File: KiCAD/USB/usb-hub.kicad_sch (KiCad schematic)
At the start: 3 parts, among them J1 Conn_01x10_Pin, J2 Conn_01x10_Pin, J3 Conn_01x04_Socket

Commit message: mmmm... usb hub controller...
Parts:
- added C1, C2, C3, C4, C5: 0.1μF, symbol Device:C_Small
- added C6: 4.7μF, symbol Device:C_Small
- added R1: 649Ω, symbol Device:R_Small
- added R2, R3, R4, R5: 10kΩ, symbol Device:R_Small
- added U1: CY7C65634-28LTXC, QFN-28, symbol 2025-09-11_12-45-01:CY7C65634-28LTXC
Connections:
- net GND: now also R1.2, U1.22 (SELFPWR), U1.29
- net USB_FNG_N: now also U1.6 (DD-[2])
- net USB_FNG_P: now also U1.7 (DD+[2])
- net USB_HOST_N: now also U1.1 (D-)
- net USB_HOST_P: now also U1.2 (D+)
- net USB_KB_N: now also U1.3 (D0-[1])
- net USB_KB_P: now also U1.4 (D0+[1])
- net VBUS: now also C6.2
- new net: R3.1, U1.23 (GANG)
- new net: C3.2, U1.9 (VCC_A)
- new net: R1.1, U1.8 (RREF)
- new net: C2.1, U1.5 (VCC_A)
- new net: R5.2, U1.24 (*OVR[2])
- new net: R4.1, U1.25 (*OVR[1])
- new net: C5.2, C6.1
- new net: C5.1, U1.27 (VCC)
- new net: R2.1, U1.17 (*RESET)
- new net: C4.1, U1.14 (VCC_A)
- new net: C1.1, U1.21 (VCC_D)
- new net +3V3: C1.2, C2.2, C3.1, C4.2, R2.2, R3.2, R4.2, R5.1, U1.28 (VREG)
- new net X_IN: U1.10 (XIN)
- new net X_OUT: U1.11 (XOUT)
- no-connect marks 0 -> 2

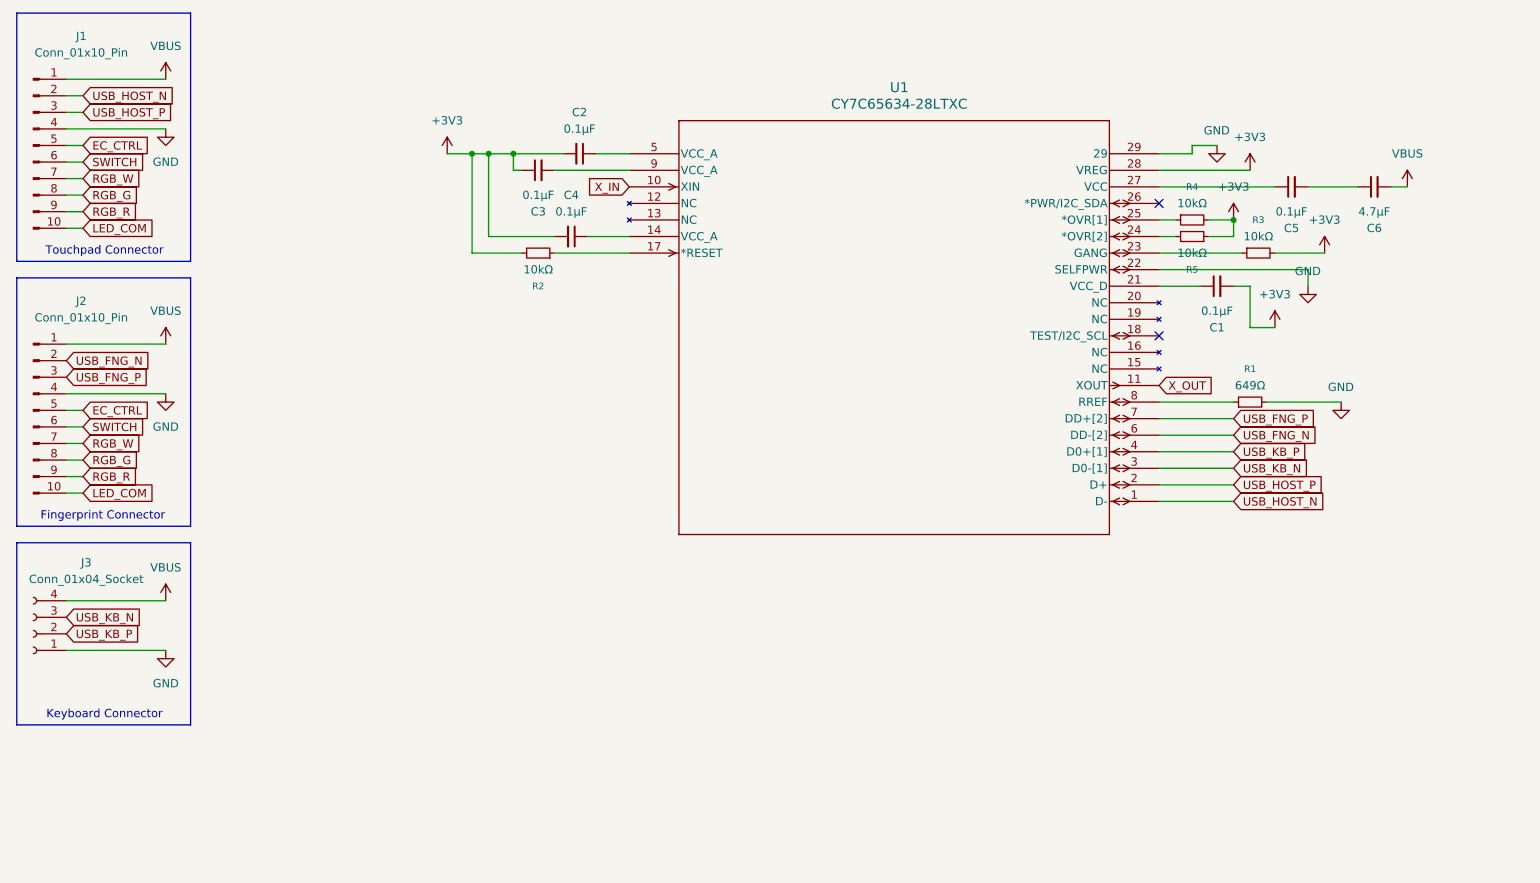
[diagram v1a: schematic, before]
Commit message: clean up schematic, add clock
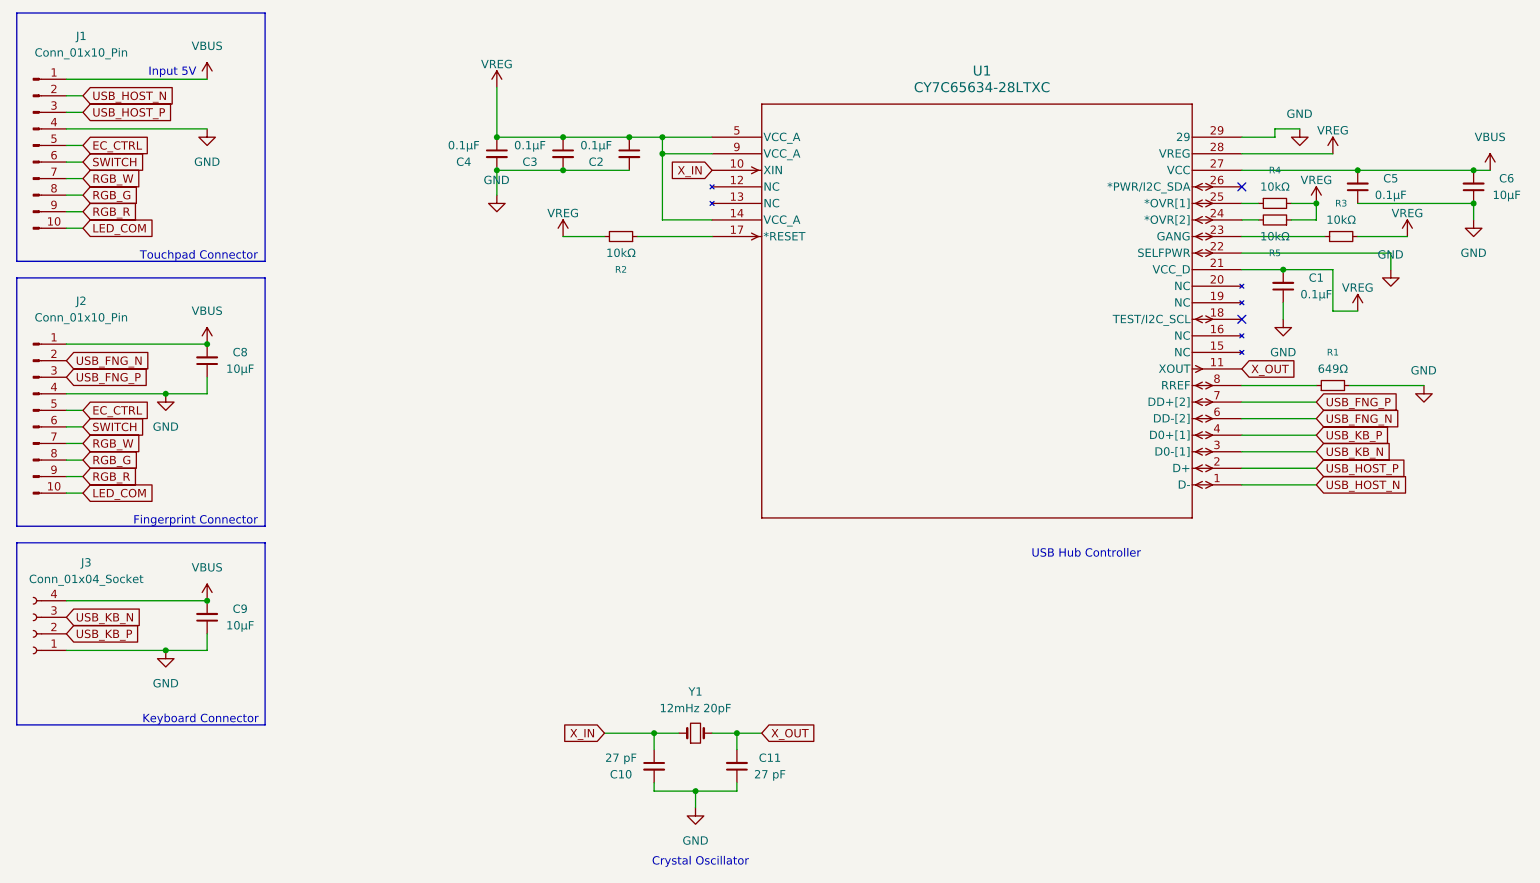
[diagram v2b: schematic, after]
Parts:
- added C10, C11: 27 pF, symbol Device:C_Small
- added C8, C9: 10μF, symbol Device:C_Small
- added Y1: 12mHz 20pF, symbol Device:Crystal_Small
- C6: value 4.7μF -> 10μF
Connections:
- net GND: now also C1.1, C2.2, C3.2, C4.2, C5.1, C6.1, C10.2, C11.1, C8.1, C9.1
- net VBUS: now also C5.2, U1.27 (VCC), C8.2, C9.2
- net X_IN: now also C10.1, Y1.1
- net X_OUT: now also C11.2, Y1.2
- net VREG: now reaches U1.9 (VCC_A)
- net VREG: now also C1.2, C2.1, C3.1, C4.1, R2.2, R3.2, R4.2, R5.1, U1.14 (VCC_A), U1.21 (VCC_D), U1.28 (VREG), U1.5 (VCC_A); no longer C3.2
- removed net +3V3: C1.2, C2.2, C3.1, C4.2, R2.2, R3.2, R4.2, R5.1, U1.28 (VREG)
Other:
- note added: "Crystal Oscillator"
- note added: "Input 5V"
- note added: "USB Hub Controller"
- moved on the sheet: C1, C2, C3, C4, C5, C6, R1, R2, R3, R4, R5, U1

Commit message: change symbol
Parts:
- removed J2: Conn_01x10_Pin, symbol Connector:Conn_01x10_Pin
- added J4: 046809610110846+, 046809610110846, symbol 046809610110846+:046809610110846+
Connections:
- net EC_CTRL: now also J4.5
- net GND: now also J3.4 (Pin_4), J4.4, J4.MP1, J4.MP2; no longer J3.1 (Pin_1)
- net LED_COM: now also J4.10
- net RGB_G: now also J4.8
- net RGB_R: now also J4.9
- net RGB_W: now also J4.7
- net SWITCH: now also J4.6
- net USB_FNG_N: now also J4.2
- net USB_FNG_P: now also J4.3
- net USB_KB_N: now also J3.2 (Pin_2); no longer J3.3 (Pin_3)
- net USB_KB_P: now also J3.3 (Pin_3); no longer J3.2 (Pin_2)
- net VBUS: now also J3.1 (Pin_1), J4.1; no longer J3.4 (Pin_4)
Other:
- moved on the sheet: C1, C10, C11, C2, C3, C4, C5, C6, C8, C9, J3, R1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

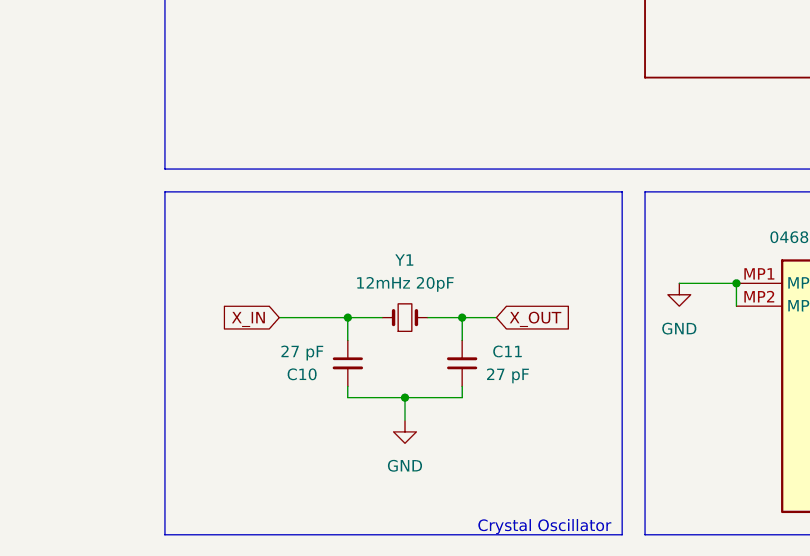
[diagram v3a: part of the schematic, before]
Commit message: fix captialization
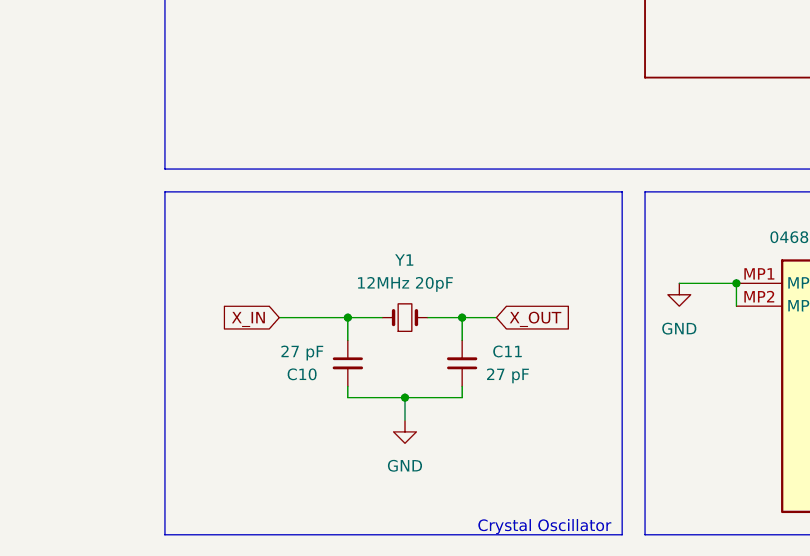
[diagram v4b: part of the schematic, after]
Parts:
- Y1: value 12mHz 20pF -> 12MHz 20pF
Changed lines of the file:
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@@
 			)
 		)
-		(property "Value" "12mHz 20pF"
+		(property "Value" "12MHz 20pF"
 			(at 92.71 127 0)
 			(effects

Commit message: stuff
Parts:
- added R6: 0Ω, symbol Device:R_Small
- J1: value Conn_01x10_Pin -> 046809610110846+ Male; footprint (none) -> Custom:Kyocera_046809610110846+_PCB_Edge
- J4: value 046809610110846+ -> 046809610110846+ Female
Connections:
- net GND: now also R6.1; no longer U1.22 (SELFPWR)
- new net: R6.2, U1.22 (SELFPWR)
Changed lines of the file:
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@@
 	(wire
 		(pts
-			(xy 208.28 73.66) (xy 208.28 66.04)
+			(xy 208.28 74.93) (xy 208.28 66.04)
 		)
 		(stroke
@@
 	(wire
 		(pts
-			(xy 212.09 73.66) (xy 212.09 72.39)
-		)
-		(stroke
-			(width 0)
-			(type default)
-		)
-	)
-	(wire
-		(pts
 			(xy 35.56 48.26) (xy 33.02 48.26)
 		)
@@
 	(wire
 		(pts
-			(xy 212.09 73.66) (xy 208.28 73.66)
+			(xy 212.09 74.93) (xy 208.28 74.93)
 		)
 		(stroke
@@
 	(wire
 		(pts
-			(xy 193.04 63.5) (xy 215.9 63.5)
+			(xy 193.04 63.5) (xy 209.55 63.5)
 		)
 		(stroke
@@
 	(wire
 		(pts
+			(xy 214.63 63.5) (xy 218.44 63.5)
+		)
+		(stroke
+			(width 0)
+			(type default)
+		)
+	)
+	(wire
+		(pts
 			(xy 35.56 45.72) (xy 33.02 45.72)
 		)
@@
 	(wire
 		(pts
-			(xy 215.9 66.04) (xy 215.9 63.5)
+			(xy 218.44 66.04) (xy 218.44 63.5)
 		)
 		(stroke
@@
 			)
 		)
-		(property "Value" "046809610110846+"
+		(property "Value" "046809610110846+ Female"
 			(at 142.24 121.92 0)
 			(effects
@@
 		(dnp no)
 		(property "Reference" "C11"
-			(at 104.1337 134.62 0)
+			(at 104.14 136.652 0)
 			(effects
 				(font
@@
 		)
 		(property "Value" "27 pF"
-			(at 104.1337 137.16 0)
+			(at 104.394 134.62 0)
 			(effects
 				(font
@@
 	)
 	(symbol
+		(lib_id "Device:R_Small")
+		(at 212.09 63.5 270)
+		(mirror x)
+		(unit 1)
+		(exclude_from_sim no)
+		(in_bom yes)
+		(on_board yes)
+		(dnp no)
+		(property "Reference" "R6"
+			(at 212.09 68.58 90)
+			(effects
+				(font
+					(size 1.016 1.016)
+				)
+			)
+		)
+		(property "Value" "0Ω"
+			(at 212.09 66.04 90)
+			(effects
+				(font
+					(size 1.27 1.27)
+				)
+			)
+		)
+		(property "Footprint" ""
+			(at 212.09 63.5 0)
+			(effects
+				(font
+					(size 1.27 1.27)
+				)
+				(hide yes)
+			)
+		)
+		(property "Datasheet" "~"
+			(at 212.09 63.5 0)
+			(effects
+				(font
+					(size 1.27 1.27)
+				)
+				(hide yes)
+			)
+		)
+		(property "Description" "Resistor, small symbol"
+			(at 212.09 63.5 0)
+			(effects
+				(font
+					(size 1.27 1.27)
+				)
+				(hide yes)
+			)
+		)
+		(pin "2"
+		)
+		(pin "1"
+		)
+		(instances
+			(project "usb-hub"
+				(path "/215ab3b1-85fe-4e4f-901d-105bf68c1066"
+					(reference "R6")
+					(unit 1)
+				)
+			)
+		)
+	)
+	(symbol
 		(lib_id "Device:C_Small")
 		(at 99.06 48.26 0)
@@
 	(symbol
 		(lib_id "power:+3V3")
-		(at 212.09 72.39 0)
+		(at 212.09 74.93 0)
 		(unit 1)
 		(exclude_from_sim no)
@@
 		(dnp no)
 		(property "Reference" "#PWR011"
-			(at 212.09 76.2 0)
+			(at 212.09 78.74 0)
 			(effects
 				(font
@@
 		)
 		(property "Value" "VREG"
-			(at 212.09 68.834 0)
+			(at 212.09 71.374 0)
 			(effects
 				(font
@@
 		)
 		(property "Footprint" ""
-			(at 212.09 72.39 0)
+			(at 212.09 74.93 0)
 			(effects
 				(font
@@
 		)
 		(property "Datasheet" ""
-			(at 212.09 72.39 0)
+			(at 212.09 74.93 0)
 			(effects
 				(font
@@
 		)
 		(property "Description" "Power symbol creates a global label with name \"+3V3\""
-			(at 212.09 72.39 0)
+			(at 212.09 74.93 0)
 			(effects
 				(font
@@
 	(symbol
 		(lib_id "power:GND")
-		(at 215.9 66.04 0)
+		(at 218.44 66.04 0)
 		(unit 1)
 		(exclude_from_sim no)
@@
 		(dnp no)
 		(property "Reference" "#PWR03"
-			(at 215.9 72.39 0)
+			(at 218.44 72.39 0)
 			(effects
 				(font
@@
 		)
 		(property "Value" "GND"
-			(at 213.868 63.754 0)
+			(at 216.408 63.754 0)
 			(effects
 				(font
@@
 		)
 		(property "Footprint" ""
-			(at 215.9 66.04 0)
+			(at 218.44 66.04 0)
 			(effects
 				(font
@@
 		)
 		(property "Datasheet" ""
-			(at 215.9 66.04 0)
+			(at 218.44 66.04 0)
 			(effects
 				(font
@@
 		)
 		(property "Description" "Power symbol creates a global label with name \"GND\" , ground"
-			(at 215.9 66.04 0)
+			(at 218.44 66.04 0)
 			(effects
 				(font
@@
 			)
 		)
-		(property "Value" "Conn_01x10_Pin"
-			(at 35.306 31.496 0)
+		(property "Value" "046809610110846+ Male"
+			(at 38.608 31.496 0)
 			(effects
 				(font
@@
 			)
 		)
-		(property "Footprint" ""
+		(property "Footprint" "Custom:Kyocera_046809610110846+_PCB_Edge"
 			(at 27.94 45.72 0)
 			(effects

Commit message: stuffs
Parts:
- removed Y1: 12MHz 20pF, symbol Device:Crystal_Small
- added R7: 1kΩ, Resistor_SMD:R_0402_1005Metric, symbol Device:R_Small
- added Y1: 12MHz 20pF, Crystal:Crystal_SMD_Abracon_ABM3B-4Pin_5.0x3.2mm, symbol Device:Crystal_GND24
- C1, C2, C3, C4, C5, C6, C8, C9: footprint (none) -> Capacitor_SMD:C_01005_0402Metric
- C10, C11: value 27 pF -> 30 pF; footprint (none) -> Capacitor_SMD:C_01005_0402Metric
- J3: footprint Connector_Wire:SolderWire-0.1sqmm_1x04_P3.6mm_D0.4mm_OD1mm -> Connector_FFC-FPC:Amphenol_F32Q-1A7x1-11004_1x04-1MP_P0.5mm_Horizontal
- R1, R2, R3, R4, R5, R6: footprint (none) -> Resistor_SMD:R_0402_1005Metric
- U1: footprint QFN-28 -> footprints:QFN-28
- renumbered J4 to J2
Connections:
- net GND: now also Y1.2, Y1.4
- net X_IN: now also Y1.1
- net X_OUT: now also R7.1; no longer C11.2
- new net: C11.2, R7.2, Y1.3
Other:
- note added: "C(L)=2*(C(Xtal)-C(Stray))=2*(20-4)=32pF->33pF"
- note added: "Crystal"
- note removed: "Crystal Oscillator"

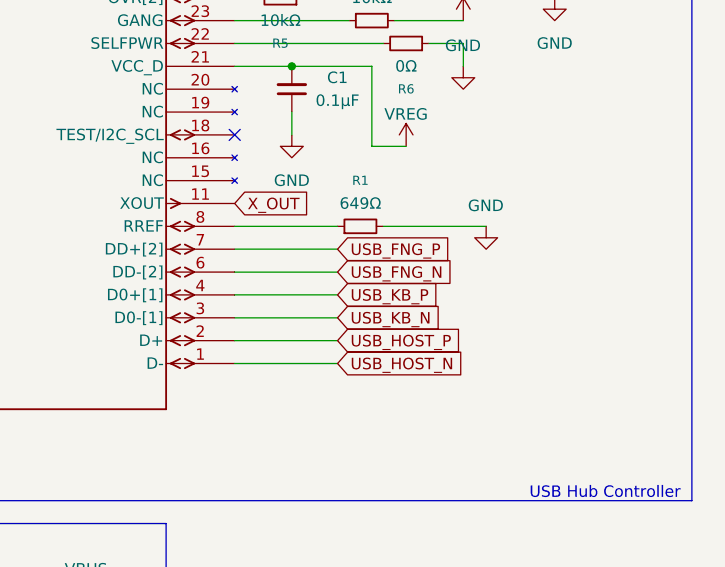
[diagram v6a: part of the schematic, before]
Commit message: Finish USB hub pcb
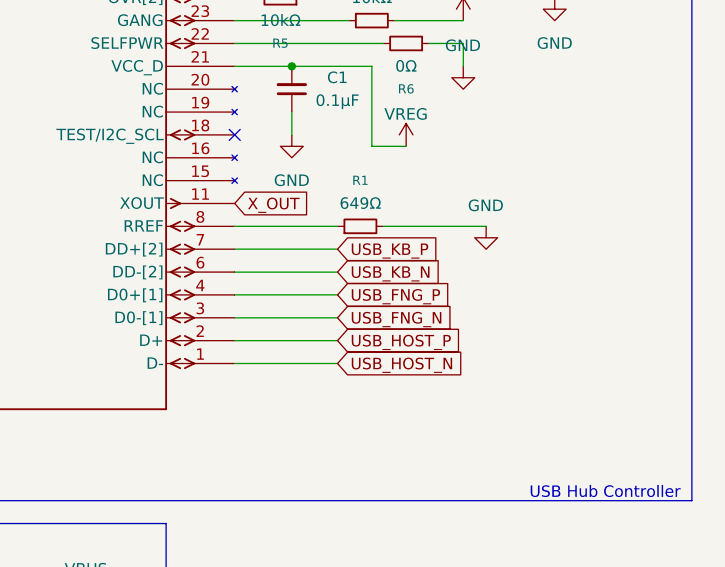
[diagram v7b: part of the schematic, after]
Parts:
- J2: footprint 046809610110846 -> SamacSys_Parts:046809610110846
- J3: footprint Connector_FFC-FPC:Amphenol_F32Q-1A7x1-11004_1x04-1MP_P0.5mm_Horizontal -> Custom:4 pad
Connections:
- net USB_FNG_N: now also U1.3 (D0-[1]); no longer U1.6 (DD-[2])
- net USB_FNG_P: now also U1.4 (D0+[1]); no longer U1.7 (DD+[2])
- net USB_KB_N: now also U1.6 (DD-[2]); no longer U1.3 (D0-[1])
- net USB_KB_P: now also U1.7 (DD+[2]); no longer U1.4 (D0+[1])
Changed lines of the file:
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@@
 	(global_label "USB_FNG_N"
 		(shape input)
-		(at 204.47 88.9 0)
+		(at 204.47 93.98 0)
 		(fields_autoplaced yes)
 		(effects
@@
 		)
 		(property "Intersheetrefs" "${INTERSHEET_REFS}"
-			(at 218.22 88.9 0)
+			(at 218.22 93.98 0)
 			(effects
 				(font
@@
 	(global_label "USB_KB_P"
 		(shape input)
-		(at 204.47 91.44 0)
+		(at 204.47 86.36 0)
 		(fields_autoplaced yes)
 		(effects
@@
 		)
 		(property "Intersheetrefs" "${INTERSHEET_REFS}"
-			(at 217.0104 91.44 0)
+			(at 217.0104 86.36 0)
 			(effects
 				(font
@@
 	(global_label "USB_FNG_P"
 		(shape input)
-		(at 204.47 86.36 0)
+		(at 204.47 91.44 0)
 		(fields_autoplaced yes)
 		(effects
@@
 		)
 		(property "Intersheetrefs" "${INTERSHEET_REFS}"
-			(at 218.1595 86.36 0)
+			(at 218.1595 91.44 0)
 			(effects
 				(font
@@
 	(global_label "USB_KB_N"
 		(shape input)
-		(at 204.47 93.98 0)
+		(at 204.47 88.9 0)
 		(fields_autoplaced yes)
 		(effects
@@
 		)
 		(property "Intersheetrefs" "${INTERSHEET_REFS}"
-			(at 217.0709 93.98 0)
+			(at 217.0709 88.9 0)
 			(effects
 				(font
@@
 			)
 		)
-		(property "Footprint" "046809610110846"
+		(property "Footprint" "SamacSys_Parts:046809610110846"
 			(at 151.13 221.92 0)
 			(effects
@@
 			)
 		)
-		(property "Footprint" "Connector_FFC-FPC:Amphenol_F32Q-1A7x1-11004_1x04-1MP_P0.5mm_Horizontal"
+		(property "Footprint" "Custom:4 pad"
 			(at 27.94 77.47 0)
 			(effects
